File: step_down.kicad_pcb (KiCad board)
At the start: 2 copper layers, 80 x 50 mm, 69 parts, among them U1 L5009

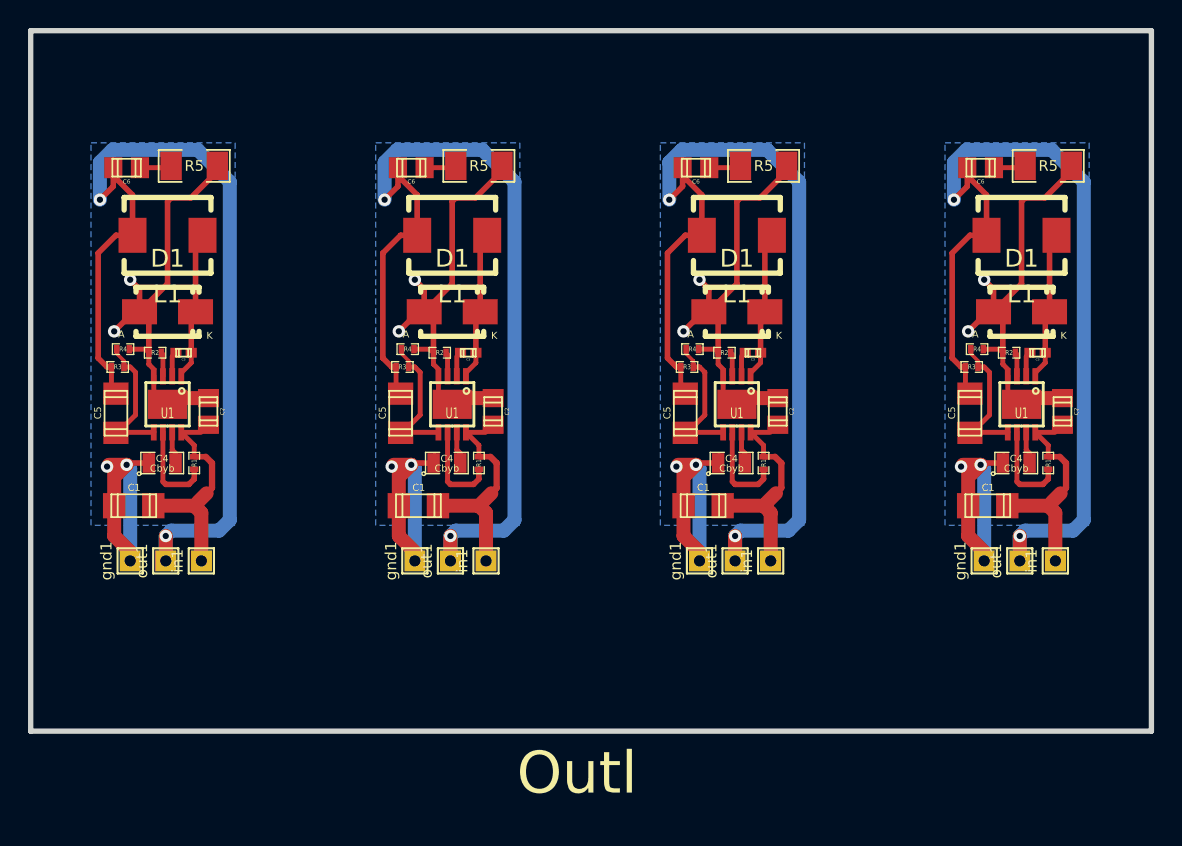
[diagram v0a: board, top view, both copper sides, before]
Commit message: bugs gefixt. fertigungsdaten hinzugefügt
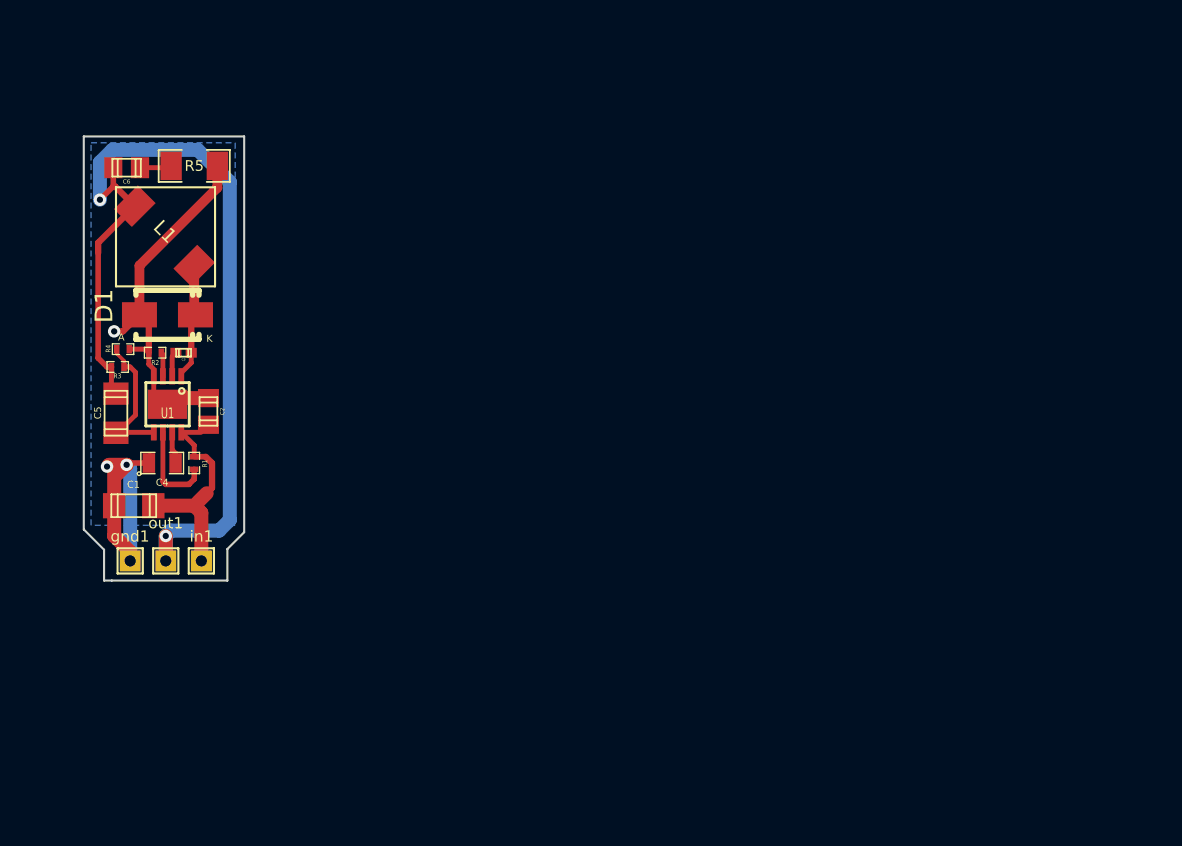
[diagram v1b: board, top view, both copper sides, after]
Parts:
- removed the C1 at (194.1, 135.5)
- removed the C1 at (214.4, 135.5)
- removed the C1 at (173.7, 135.5)
- removed the C2 at (199.4, 128.8)
- removed the C2 at (219.7, 128.8)
- removed the C2 at (179.1, 128.8)
- removed the C3 at (197.6, 124.6)
- removed the C3 at (217.9, 124.6)
- removed the C3 at (177.3, 124.6)
- removed the C4 at (196.1, 132.5)
- removed the C4 at (216.4, 132.5)
- removed the C4 at (175.8, 132.5)
- removed the C5 at (192.8, 128.9)
- removed the C5 at (213.1, 128.9)
- removed the C5 at (172.5, 128.9)
- removed the C6 at (193.5, 111.4)
- removed the C6 at (213.9, 111.4)
- removed the C6 at (173.2, 111.4)
- removed the D1 at (196.5, 121.7)
- removed the D1 at (216.8, 121.7)
- removed the D1 at (176.1, 121.7)
- removed the L1 at (196.5, 116.2)
- removed the L1 at (216.8, 116.2)
- removed the L1 at (176.1, 116.2)
- removed the L1 at (155.8, 116.2)
- removed Outl: EuroBoard_viertel_Type-I_80mmX50mm, EuroBoard_Outline:EuroBoard_viertel_Type-I_80mmX50mm
- removed the R1 at (198.4, 132.5)
- removed the R1 at (218.7, 132.5)
- removed the R1 at (178.1, 132.5)
- removed the R2 at (195.6, 124.6)
- removed the R2 at (215.9, 124.6)
- removed the R2 at (175.3, 124.6)
- removed the R3 at (192.9, 125.6)
- removed the R3 at (213.2, 125.6)
- removed the R3 at (172.6, 125.6)
- removed the R4 at (193.3, 124.3)
- removed the R4 at (213.6, 124.3)
- removed the R4 at (173.0, 124.3)
- removed the R5 at (198.4, 111.3)
- removed the R5 at (218.7, 111.3)
- removed the R5 at (178.1, 111.3)
- removed the U1 at (196.5, 128.3)
- removed the U1 at (216.8, 128.3)
- removed the U1 at (176.1, 128.3)
- removed the gnd1 at (193.8, 139.4)
- removed the gnd1 at (214.1, 139.4)
- removed the gnd1 at (173.5, 139.4)
- removed the in1 at (198.9, 139.4)
- removed the in1 at (219.2, 139.4)
- removed the in1 at (178.6, 139.4)
- removed the out1 at (196.3, 139.4)
- removed the out1 at (216.7, 139.4)
- removed the out1 at (176.0, 139.4)
- added L1: INDUCTOR_SMALL, toni:SRR7032_Series, F.Cu at (157.1, 117.7)
- moved D1 0.22 mm to (155.8, 121.9)
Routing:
- net Net-(C5-Pad1): track 277.6 -> 67.2 mm, vias 8 -> 2
- net GND: track 198.3 -> 47.8 mm, vias 16 -> 3
- net Net-(C1-Pad1): track 65.7 -> 16.4 mm
- net Net-(C3-Pad2): track 42.8 -> 8.93 mm
- net Net-(C5-Pad2): track 40.6 -> 10.2 mm
- net Net-(R1-Pad2): track 26.7 -> 6.68 mm
- net Net-(C4-Pad2): track 9.17 -> 2.29 mm
- net Net-(C6-Pad2): track 9.10 -> 2.28 mm
- net Net-(C3-Pad1): track 7.17 -> 1.79 mm
- net Net-(R2-Pad1): track 6.92 -> 1.73 mm
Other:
- board size 80 x 50 mm -> 11.5 x 31.7 mm
